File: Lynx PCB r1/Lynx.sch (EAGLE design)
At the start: 111 parts, among them IC1 LM321MF, IC3 ICL7660, Q1 8MHz

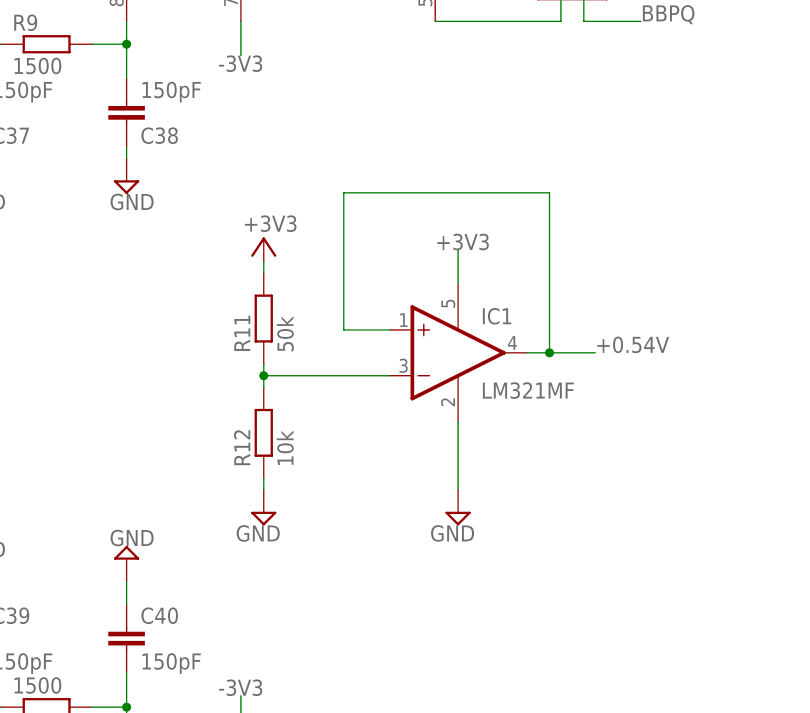
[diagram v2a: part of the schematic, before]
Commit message: Final PCB r1 commit
Fixed lots of little thing.
Gerbers checked
Fixed 0.54v generation oopsie (inverting and non-inverting terminals
wrong way around)
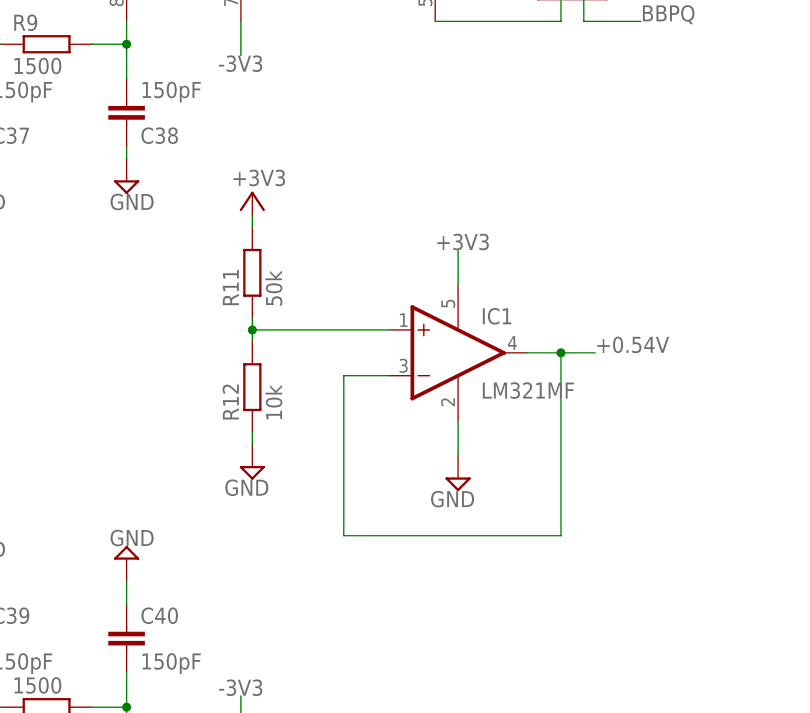
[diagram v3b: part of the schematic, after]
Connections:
- net +0.54V: now also IC1.-IN; no longer IC1.+IN
- net N$42: now also IC1.+IN; no longer IC1.-IN
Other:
- moved on the sheet: R11, R12
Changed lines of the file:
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@@
 <instance part="JP10" gate="G$1" x="-245.11" y="-154.94" rot="R180"/>
 <instance part="IC1" gate="G$1" x="85.09" y="-26.67"/>
-<instance part="R11" gate="G$1" x="63.5" y="-22.86" rot="R90"/>
-<instance part="R12" gate="G$1" x="63.5" y="-35.56" rot="R90"/>
-<instance part="+3V17" gate="G$1" x="63.5" y="-13.97" smashed="yes">
-<attribute name="VALUE" x="67.31" y="-11.43" size="1.778" layer="96" rot="R180"/>
+<instance part="R11" gate="G$1" x="62.23" y="-17.78" rot="R90"/>
+<instance part="R12" gate="G$1" x="62.23" y="-30.48" rot="R90"/>
+<instance part="+3V17" gate="G$1" x="62.23" y="-8.89" smashed="yes">
+<attribute name="VALUE" x="66.04" y="-6.35" size="1.778" layer="96" rot="R180"/>
 </instance>
-<instance part="SUPPLY58" gate="GND" x="63.5" y="-44.45" rot="MR0"/>
-<instance part="SUPPLY59" gate="GND" x="85.09" y="-44.45" rot="MR0"/>
+<instance part="SUPPLY58" gate="GND" x="62.23" y="-39.37" rot="MR0"/>
+<instance part="SUPPLY59" gate="GND" x="85.09" y="-40.64" rot="MR0"/>
 <instance part="JP11" gate="G$1" x="-243.84" y="-168.91" rot="R180"/>
 <instance part="DAC-CLK" gate="G$1" x="-198.12" y="29.21" smashed="yes" rot="R90">
@@
 <pinref part="SUPPLY58" gate="GND" pin="GND"/>
 <pinref part="R12" gate="G$1" pin="1"/>
-<wire x1="63.5" y1="-41.91" x2="63.5" y2="-40.64" width="0.1524" layer="91"/>
+<wire x1="62.23" y1="-36.83" x2="62.23" y2="-35.56" width="0.1524" layer="91"/>
 </segment>
 <segment>
 <pinref part="IC1" gate="G$1" pin="V-"/>
 <pinref part="SUPPLY59" gate="GND" pin="GND"/>
-<wire x1="85.09" y1="-41.91" x2="85.09" y2="-34.29" width="0.1524" layer="91"/>
+<wire x1="85.09" y1="-38.1" x2="85.09" y2="-34.29" width="0.1524" layer="91"/>
 </segment>
 <segment>
@@
 <pinref part="R11" gate="G$1" pin="2"/>
 <pinref part="+3V17" gate="G$1" pin="+3V3"/>
-<wire x1="63.5" y1="-16.51" x2="63.5" y2="-17.78" width="0.1524" layer="91"/>
+<wire x1="62.23" y1="-11.43" x2="62.23" y2="-12.7" width="0.1524" layer="91"/>
 </segment>
 </net>
@@
 </segment>
 <segment>
-<pinref part="IC1" gate="G$1" pin="+IN"/>
-<wire x1="77.47" y1="-24.13" x2="72.39" y2="-24.13" width="0.1524" layer="91"/>
-<wire x1="72.39" y1="-24.13" x2="72.39" y2="-8.89" width="0.1524" layer="91"/>
-<wire x1="72.39" y1="-8.89" x2="95.25" y2="-8.89" width="0.1524" layer="91"/>
-<wire x1="95.25" y1="-8.89" x2="95.25" y2="-26.67" width="0.1524" layer="91"/>
 <pinref part="IC1" gate="G$1" pin="OUT"/>
-<wire x1="95.25" y1="-26.67" x2="92.71" y2="-26.67" width="0.1524" layer="91"/>
-<wire x1="95.25" y1="-26.67" x2="100.33" y2="-26.67" width="0.1524" layer="91"/>
-<junction x="95.25" y="-26.67"/>
+<wire x1="92.71" y1="-26.67" x2="96.52" y2="-26.67" width="0.1524" layer="91"/>
 <label x="100.33" y="-26.67" size="1.778" layer="95"/>
+<pinref part="IC1" gate="G$1" pin="-IN"/>
+<wire x1="96.52" y1="-26.67" x2="100.33" y2="-26.67" width="0.1524" layer="91"/>
+<wire x1="77.47" y1="-29.21" x2="72.39" y2="-29.21" width="0.1524" layer="91"/>
+<wire x1="72.39" y1="-29.21" x2="72.39" y2="-46.99" width="0.1524" layer="91"/>
+<wire x1="72.39" y1="-46.99" x2="96.52" y2="-46.99" width="0.1524" layer="91"/>
+<wire x1="96.52" y1="-46.99" x2="96.52" y2="-26.67" width="0.1524" layer="91"/>
+<junction x="96.52" y="-26.67"/>
 </segment>
 </net>
@@
 <net name="N$42" class="0">
 <segment>
-<pinref part="IC1" gate="G$1" pin="-IN"/>
-<wire x1="77.47" y1="-29.21" x2="63.5" y2="-29.21" width="0.1524" layer="91"/>
 <pinref part="R11" gate="G$1" pin="1"/>
-<wire x1="63.5" y1="-29.21" x2="63.5" y2="-27.94" width="0.1524" layer="91"/>
 <pinref part="R12" gate="G$1" pin="2"/>
-<wire x1="63.5" y1="-30.48" x2="63.5" y2="-29.21" width="0.1524" layer="91"/>
-<junction x="63.5" y="-29.21"/>
-</segment>
-</net>
+<wire x1="62.23" y1="-25.4" x2="62.23" y2="-24.13" width="0.1524" layer="91"/>
+<pinref part="IC1" gate="G$1" pin="+IN"/>
+<wire x1="62.23" y1="-24.13" x2="62.23" y2="-22.86" width="0.1524" layer="91"/>
+<wire x1="77.47" y1="-24.13" x2="62.23" y2="-24.13" width="0.1524" layer="91"/>
+<junction x="62.23" y="-24.13"/>
+</segment>
+</net>
